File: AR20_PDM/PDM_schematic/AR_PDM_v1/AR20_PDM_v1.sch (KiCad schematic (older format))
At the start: 20 parts, among them J1 S_T_?, J2 1-776163-1, U1 ACM_2020

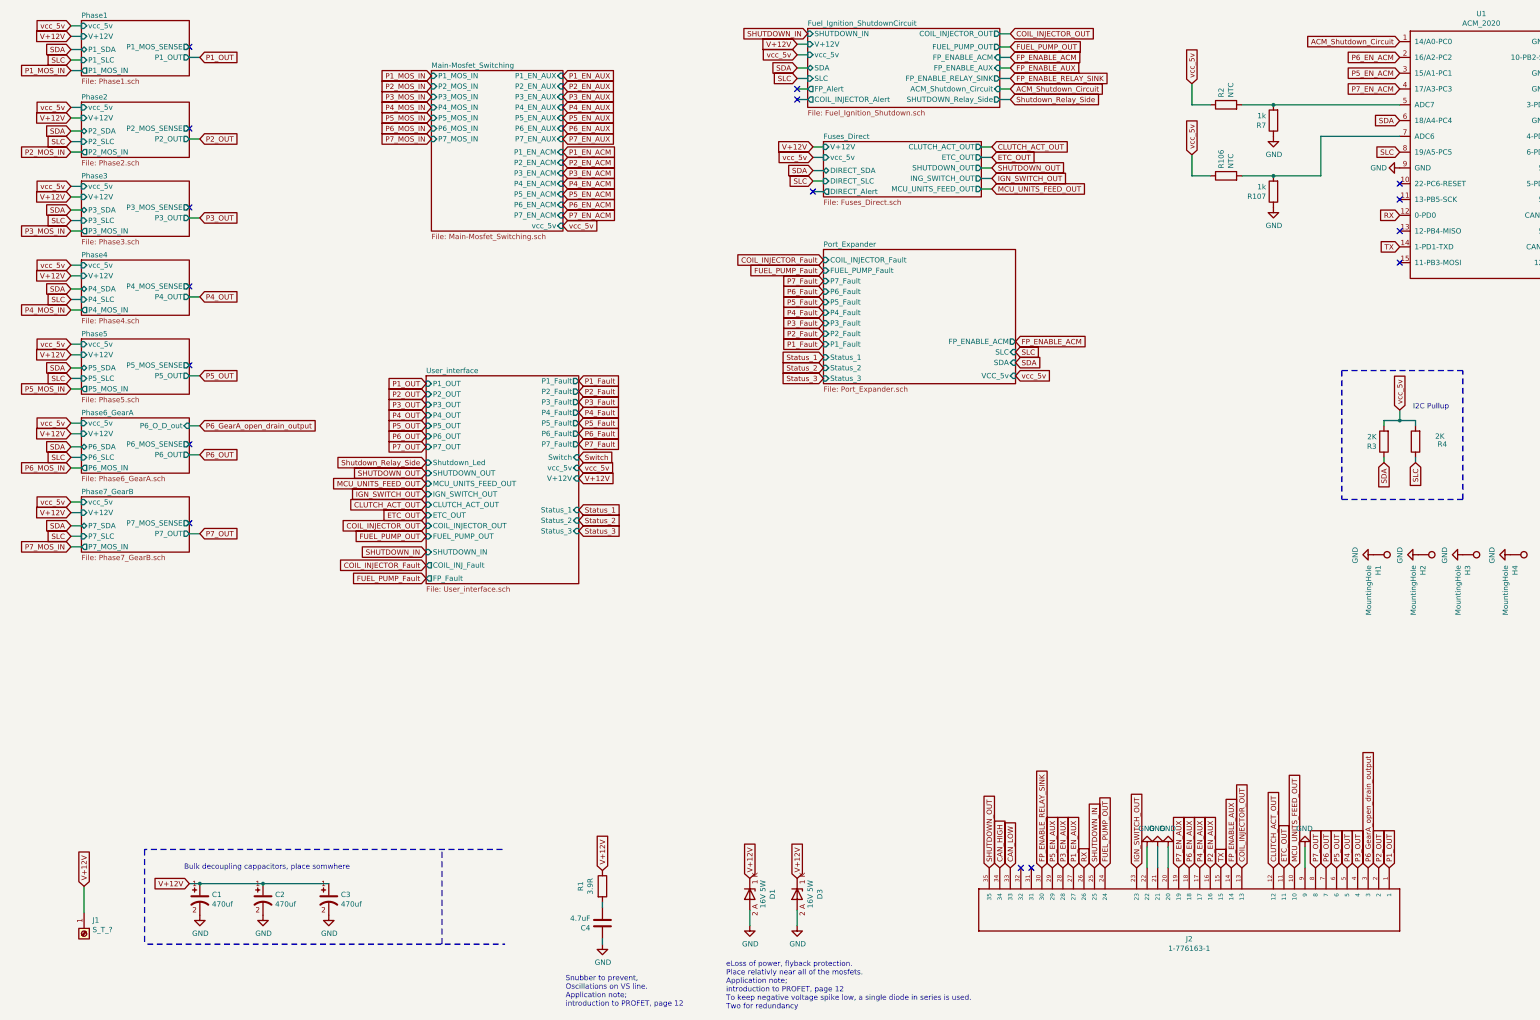
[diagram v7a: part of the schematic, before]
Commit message: PDM mostly complete
- Reverse polarity protection implemented
- All traces layed out
- final polish missing
- DRC missing
- Final check missing
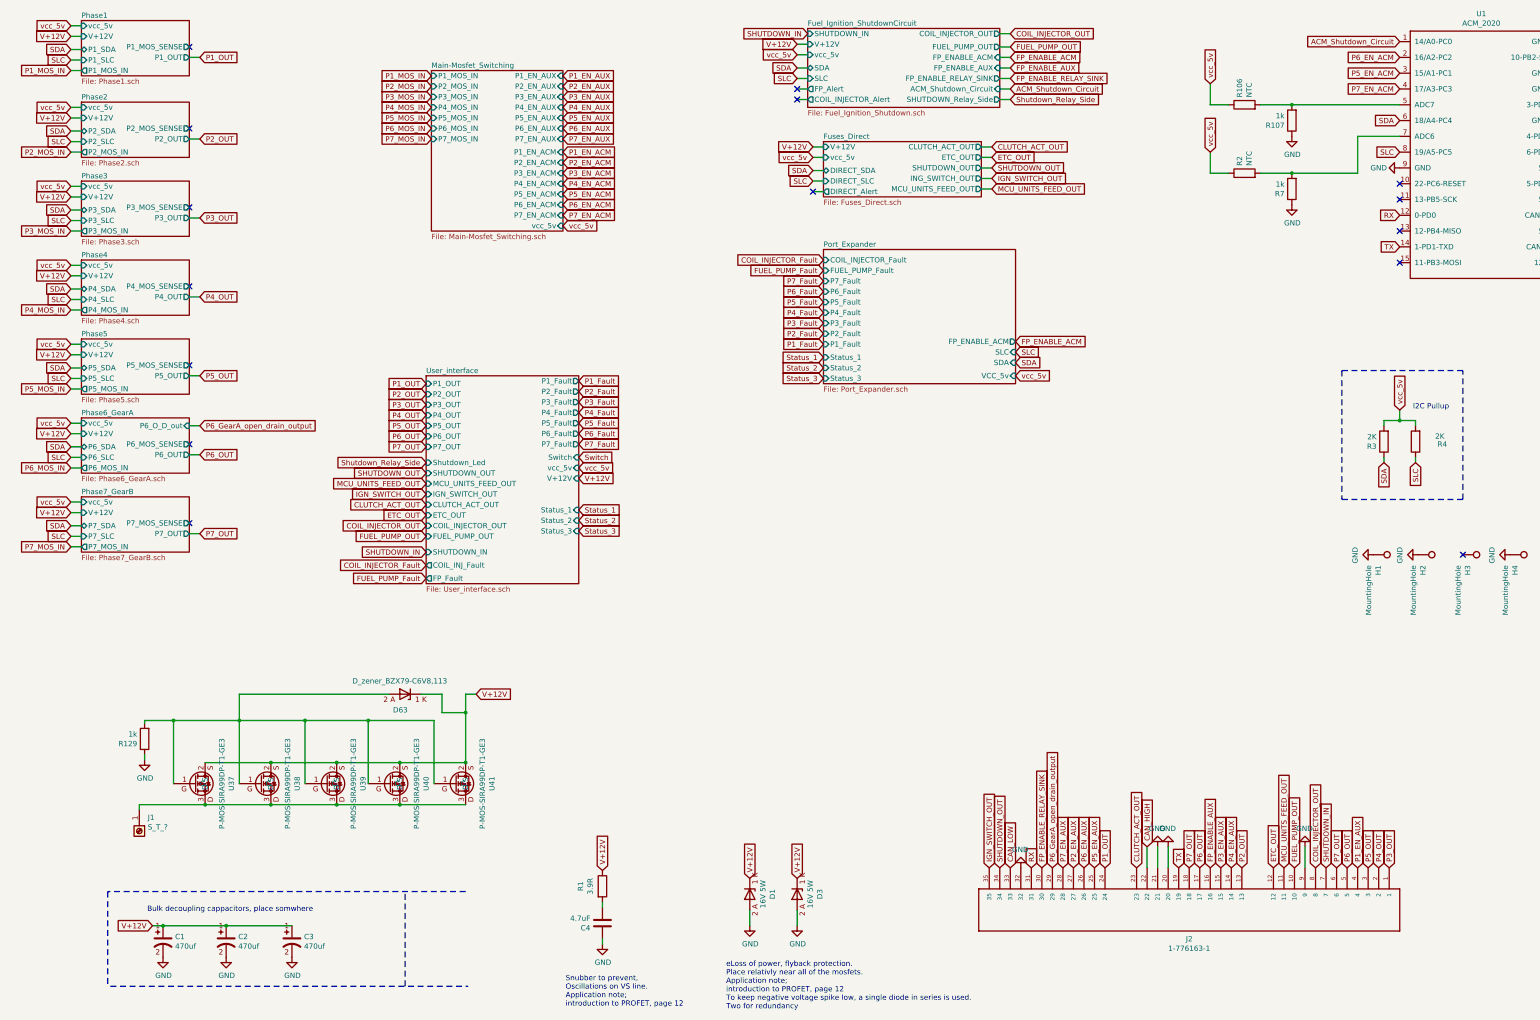
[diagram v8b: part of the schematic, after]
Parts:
- added D63: D_zener_BZX79-C6V8,113, AR_PDM_v1:D_DO-35_BZX79-C6V8,113, symbol AR20_PDM_v1-rescue:D_zener_BZX79-C6V8,113
- added R129: 1k, Resistor_SMD:R_0603_1608Metric, symbol AR20_PDM_v1-rescue:R-Device
- added U37, U38, U39, U40, U41: P-MOS-SIRA99DP-T1-GE3, AR_PDM_v1:P-MOS-SIRA99DP-T1-GE3, symbol AR20_PDM_v1-rescue:P-MOS-SIRA99DP-T1-GE3
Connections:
- net CAN_HIGH: now also J2.22; no longer J2.34
- net CLUTCH_ACT_OUT: now also J2.23; no longer J2.12
- net COIL_INJECTOR_OUT: now also J2.8; no longer J2.13
- net ETC_OUT: now also J2.12; no longer J2.11
- net FP_ENABLE_AUX: now also J2.16; no longer J2.14
- net FUEL_PUMP_OUT: now also J2.10; no longer J2.24
- net GND: now also J2.32, R129.1; no longer H3.1, J2.22
- net IGN_SWITCH_OUT: now also J2.35; no longer J2.23
- net MCU_UNITS_FEED_OUT: now also J2.11; no longer J2.10
- net P1_EN_AUX: now also J2.4; no longer J2.27
- net P1_OUT: now also J2.24; no longer J2.1
- net P2_EN_AUX: now also J2.27; no longer J2.16
- net P2_OUT: now also J2.13; no longer J2.2
- net P3_EN_AUX: now also J2.15; no longer J2.28
- net P3_OUT: now also J2.1; no longer J2.4
- net P4_EN_AUX: now also J2.14; no longer J2.17
- net P4_OUT: now also J2.2; no longer J2.5
- net P5_EN_AUX: now also J2.25; no longer J2.29
- net P5_OUT: now also J2.3; no longer J2.6
- net P6_EN_AUX: now also J2.26; no longer J2.18
- net P6_GearA_open_drain_output: now also J2.29; no longer J2.3
- net P6_OUT: now also J2.17, J2.5; no longer J2.7
- net P7_EN_AUX: now also J2.28; no longer J2.19
- net P7_OUT: now also J2.18, J2.6; no longer J2.8
- net RX: now also J2.31; no longer J2.26
- net SHUTDOWN_IN: now also J2.7; no longer J2.25
- net SHUTDOWN_OUT: now also J2.34; no longer J2.35
- net TX: now also J2.19; no longer J2.15
- net V+12V: now also D63.1 (K), U37.2 (S), U38.2 (S), U39.2 (S), U40.2 (S), U41.2 (S); no longer J1.1 (Pin_1)
- net at R2.2, R7.2: now also U1.7 (ADC6); no longer U1.5 (ADC7)
- net at R106.2, R107.2: now also U1.5 (ADC7); no longer U1.7 (ADC6)
- new net: J1.1 (Pin_1), U37.3 (D), U38.3 (D), U39.3 (D), U40.3 (D), U41.3 (D)
- new net: D63.2 (A), R129.2, U37.1 (G), U38.1 (G), U39.1 (G), U40.1 (G), U41.1 (G)
- no-connect marks 17 -> 16
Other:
- moved on the sheet: C1, C2, C3, J1, R106, R107, R2, R7
